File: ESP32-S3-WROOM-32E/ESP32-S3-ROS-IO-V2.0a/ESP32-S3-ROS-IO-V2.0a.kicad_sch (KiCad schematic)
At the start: 45 parts, among them J1 Conn_01x22_Socket, J16 XT60-M, J17 XT60-M, J2 Conn_01x22_Socket, J3 Conn_01x22_Socket, J4 Conn_01x22_Socket, J5 Conn_01x02_Pin, SW1 SW1, SW2 SW2, SW3 SW3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

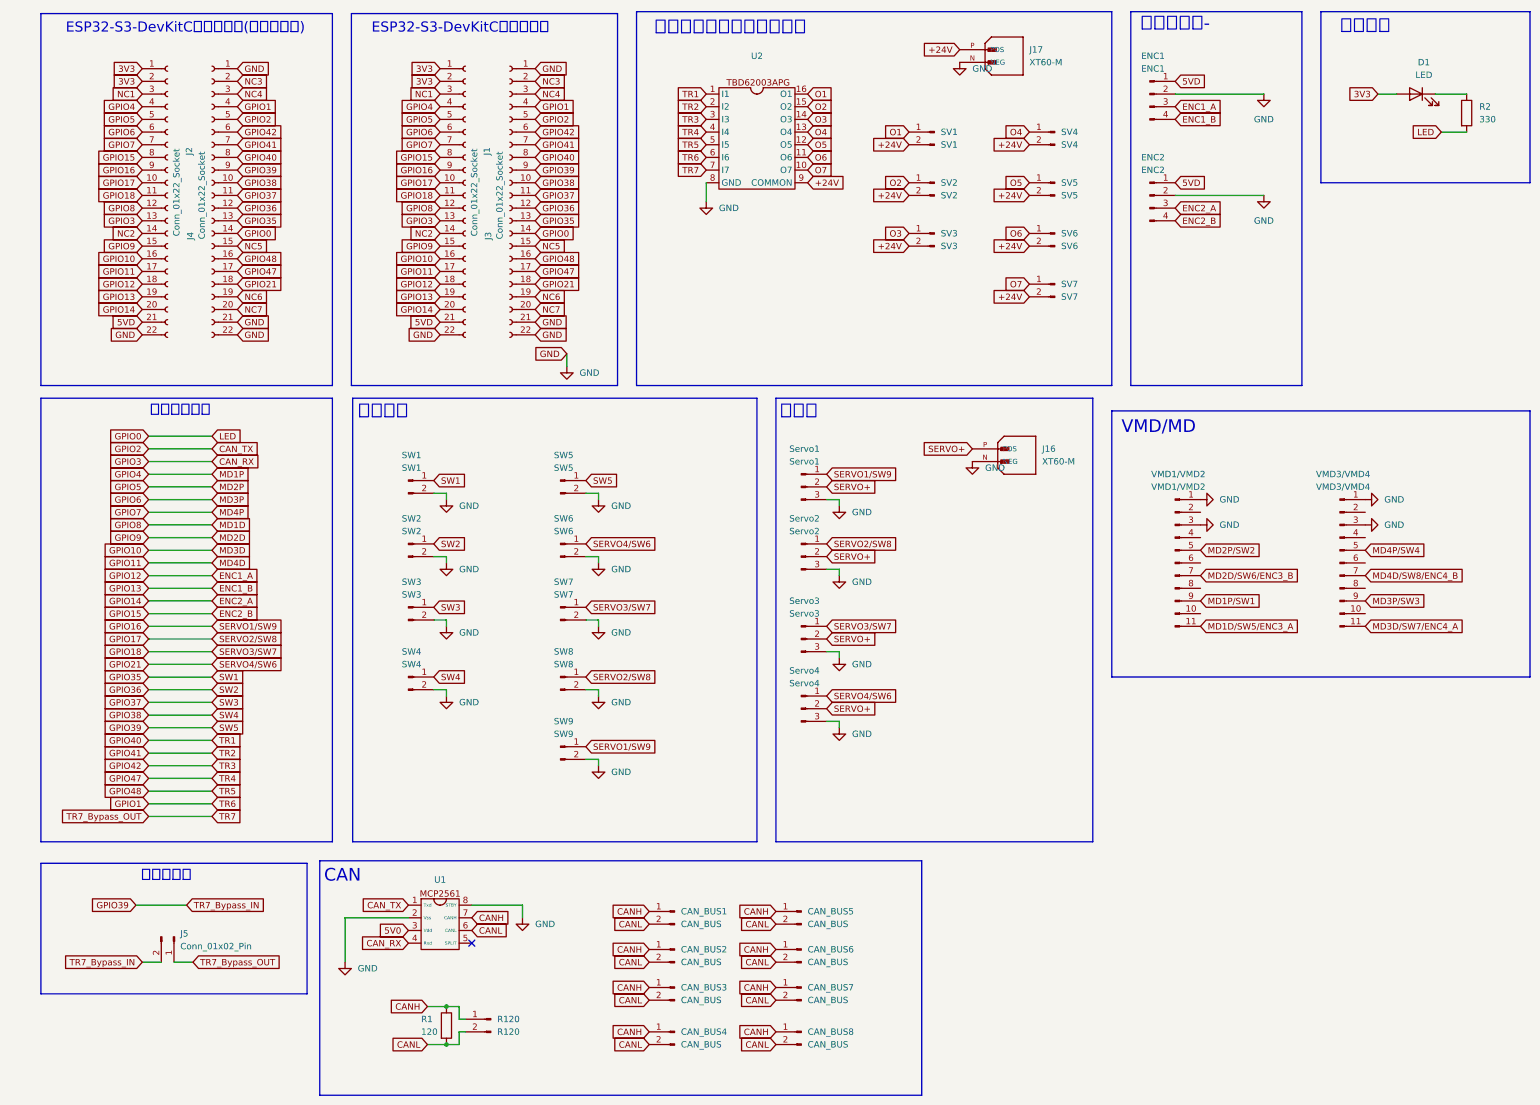
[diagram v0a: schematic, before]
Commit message: アクチュエーター数変更
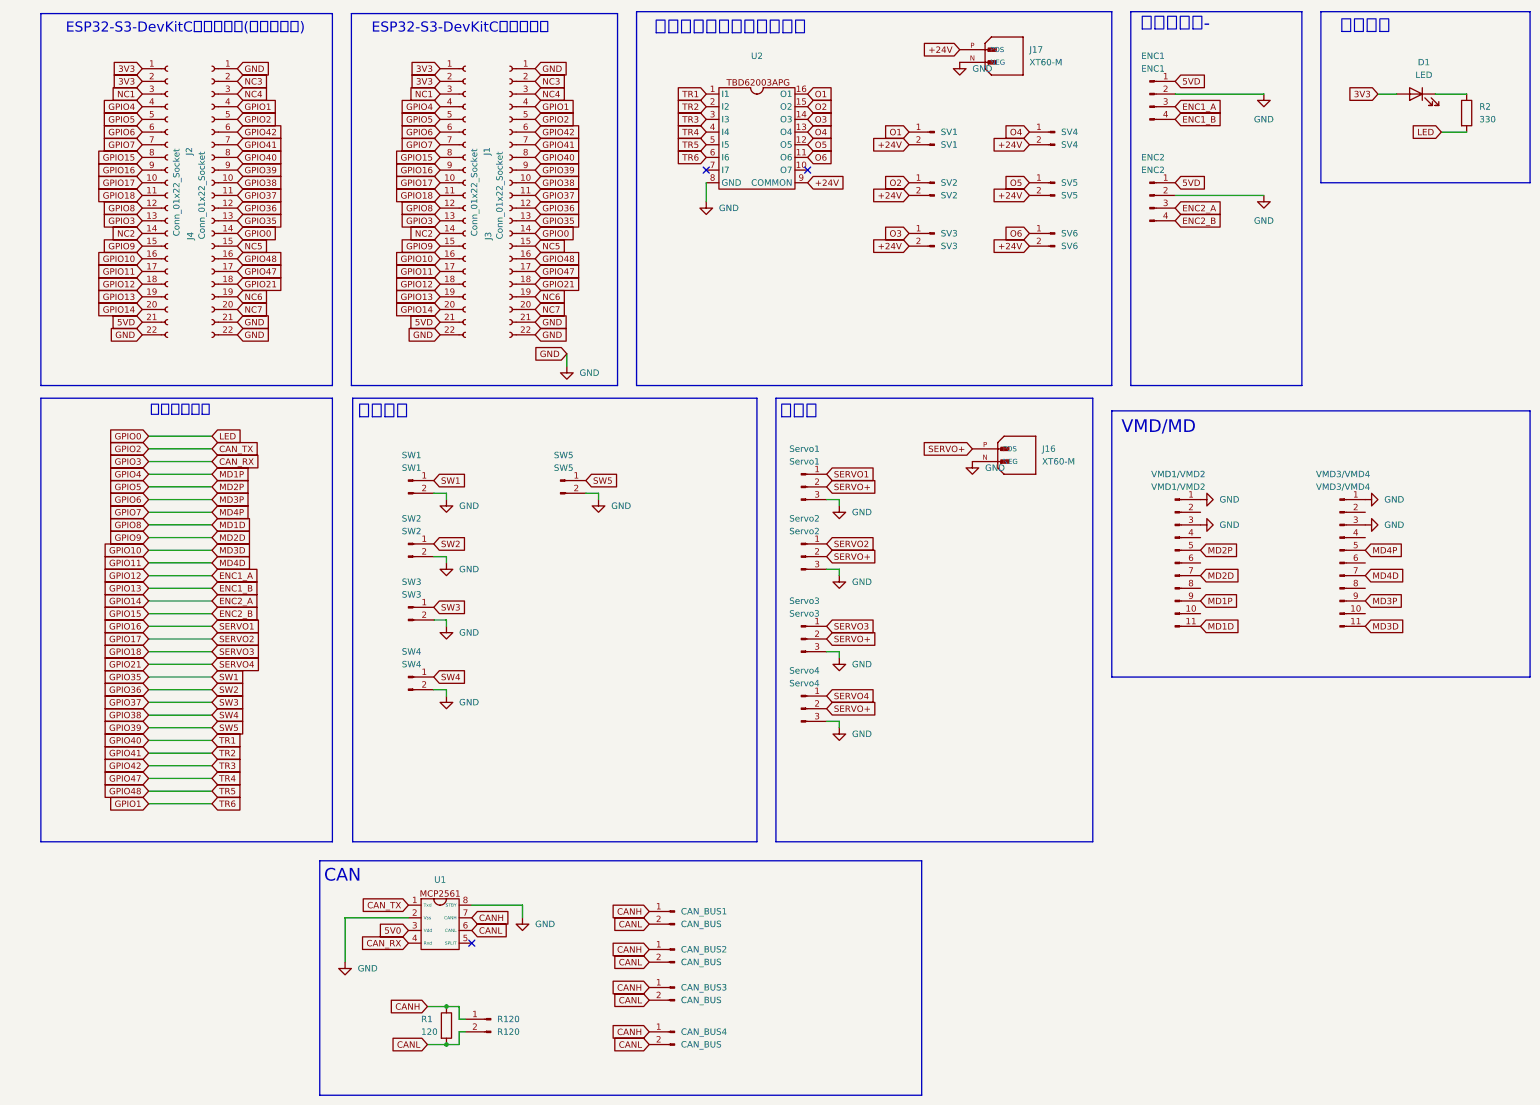
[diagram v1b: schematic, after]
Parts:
- removed CAN_BUS5, CAN_BUS6, CAN_BUS7, CAN_BUS8: CAN_BUS, Connector_JST:JST_XH_B2B-XH-A_1x02_P2.50mm_Vertical, symbol Connector:Conn_01x02_Pin
- removed J5: Conn_01x02_Pin, Connector_PinHeader_2.54mm:PinHeader_1x02_P2.54mm_Vertical, symbol Connector:Conn_01x02_Pin
- removed SV7: SV7, Connector_JST:JST_XH_B2B-XH-A_1x02_P2.50mm_Vertical, symbol Connector:Conn_01x02_Pin
- removed SW6: SW6, Connector_JST:JST_XH_B2B-XH-A_1x02_P2.50mm_Vertical, symbol Connector:Conn_01x02_Pin
- removed SW7: SW7, Connector_JST:JST_XH_B2B-XH-A_1x02_P2.50mm_Vertical, symbol Connector:Conn_01x02_Pin
- removed SW8: SW8, Connector_JST:JST_XH_B2B-XH-A_1x02_P2.50mm_Vertical, symbol Connector:Conn_01x02_Pin
- removed SW9: SW9, Connector_JST:JST_XH_B2B-XH-A_1x02_P2.50mm_Vertical, symbol Connector:Conn_01x02_Pin
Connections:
- net MD1D/SW5/ENC3_A is gone; now on net GPIO8: VMD1/VMD2.11 (Pin_11)
- net MD1P/SW1 is gone; now on net GPIO4: VMD1/VMD2.9 (Pin_9)
- net MD2D/SW6/ENC3_B is gone; now on net GPIO9: VMD1/VMD2.7 (Pin_7)
- net MD2P/SW2 is gone; now on net GPIO5: VMD1/VMD2.5 (Pin_5)
- net MD3D/SW7/ENC4_A is gone; now on net GPIO10: VMD3/VMD4.11 (Pin_11)
- net MD3P/SW3 is gone; now on net GPIO6: VMD3/VMD4.9 (Pin_9)
- net MD4D/SW8/ENC4_B is gone; now on net GPIO11: VMD3/VMD4.7 (Pin_7)
- net MD4P/SW4 is gone; now on net GPIO7: VMD3/VMD4.5 (Pin_5)
- net O7: no longer names the net of U2.10 (O7)
- net TR7: no longer names the net of U2.7 (I7)
- no-connect marks 1 -> 3
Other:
- note removed: "バイパス用"

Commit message: 製造ファイル出力
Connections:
- net 5VD is gone; now on net 5V0: ENC1.1 (Pin_1), ENC2.1 (Pin_1), J1.21 (Pin_21), J2.21 (Pin_21)
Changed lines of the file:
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@@
 		)
 	)
-	(global_label "5VD"
+	(global_label "5V0"
 		(shape input)
 		(at 246.38 53.34 0)
@@
 		)
 		(property "Intersheetrefs" "${INTERSHEET_REFS}"
-			(at 252.9333 53.34 0)
+			(at 252.8728 53.34 0)
 			(effects
 				(font
@@
 		)
 	)
-	(global_label "5VD"
+	(global_label "5V0"
 		(shape input)
 		(at 246.38 33.02 0)
@@
 		)
 		(property "Intersheetrefs" "${INTERSHEET_REFS}"
-			(at 252.9333 33.02 0)
+			(at 252.8728 33.02 0)
 			(effects
 				(font
@@
 		)
 	)
-	(global_label "5VD"
+	(global_label "5V0"
 		(shape input)
 		(at 39.37 81.28 180)
@@
 		)
 		(property "Intersheetrefs" "${INTERSHEET_REFS}"
-			(at 32.8167 81.28 0)
+			(at 32.8772 81.28 0)
 			(effects
 				(font
@@
 		)
 	)
-	(global_label "5VD"
+	(global_label "5V0"
 		(shape input)
 		(at 99.06 81.28 180)
@@
 		)
 		(property "Intersheetrefs" "${INTERSHEET_REFS}"
-			(at 92.5067 81.28 0)
-			(effects
-				(font
+			(at 92.5672 81.28 0)
+			(effects
+				(font
